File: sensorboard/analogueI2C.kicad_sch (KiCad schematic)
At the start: 51 parts, among them J1 Conn_01x03, J12 Conn_01x03, J13 Conn_01x03, J2 Conn_01x03, J3 Conn_01x03, J4 Conn_01x03, J5 Conn_01x03, J6 Conn_01x03, J7 Conn_01x03, J8 Conn_01x03, U13 ADS1219, U14 ADS1219, U15 ADS1219

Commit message: schemtiac update
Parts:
- added C25, C26, C27: 10uF, Capacitor_SMD:C_0603_1608Metric, symbol Device:C_Small
- added C28, C29, C30: 100nF, Capacitor_SMD:C_0603_1608Metric, symbol Device:C_Small
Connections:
- net +3V3: now also C25.1, C26.1, C27.1, C28.1, C29.1, C30.1
- net GND: now also C25.2, C26.2, C27.2, C28.2, C29.2, C30.2

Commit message: update
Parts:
- R29, R30, R31: value 1k -> 10k
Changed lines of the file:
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@@
     (in_bom yes) (on_board yes)
     (property "Reference" "R31" (id 0) (at 60.96 94.0816 90))
-    (property "Value" "1k" (id 1) (at 60.96 96.393 90))
+    (property "Value" "10k" (id 1) (at 60.96 96.393 90))
     (property "Footprint" "Resistor_SMD:R_0603_1608Metric" (id 2) (at 60.96 99.06 0)
       (effects (font (size 1.27 1.27)) hide)
@@
     (in_bom yes) (on_board yes)
     (property "Reference" "R30" (id 0) (at 60.96 59.7916 90))
-    (property "Value" "1k" (id 1) (at 60.96 62.103 90))
+    (property "Value" "10k" (id 1) (at 60.96 62.103 90))
     (property "Footprint" "Resistor_SMD:R_0603_1608Metric" (id 2) (at 60.96 64.77 0)
       (effects (font (size 1.27 1.27)) hide)
@@
     (in_bom yes) (on_board yes)
     (property "Reference" "R29" (id 0) (at 60.96 25.5016 90))
-    (property "Value" "1k" (id 1) (at 60.96 27.813 90))
+    (property "Value" "10k" (id 1) (at 60.96 27.813 90))
     (property "Footprint" "Resistor_SMD:R_0603_1608Metric" (id 2) (at 60.96 30.48 0)
       (effects (font (size 1.27 1.27)) hide)

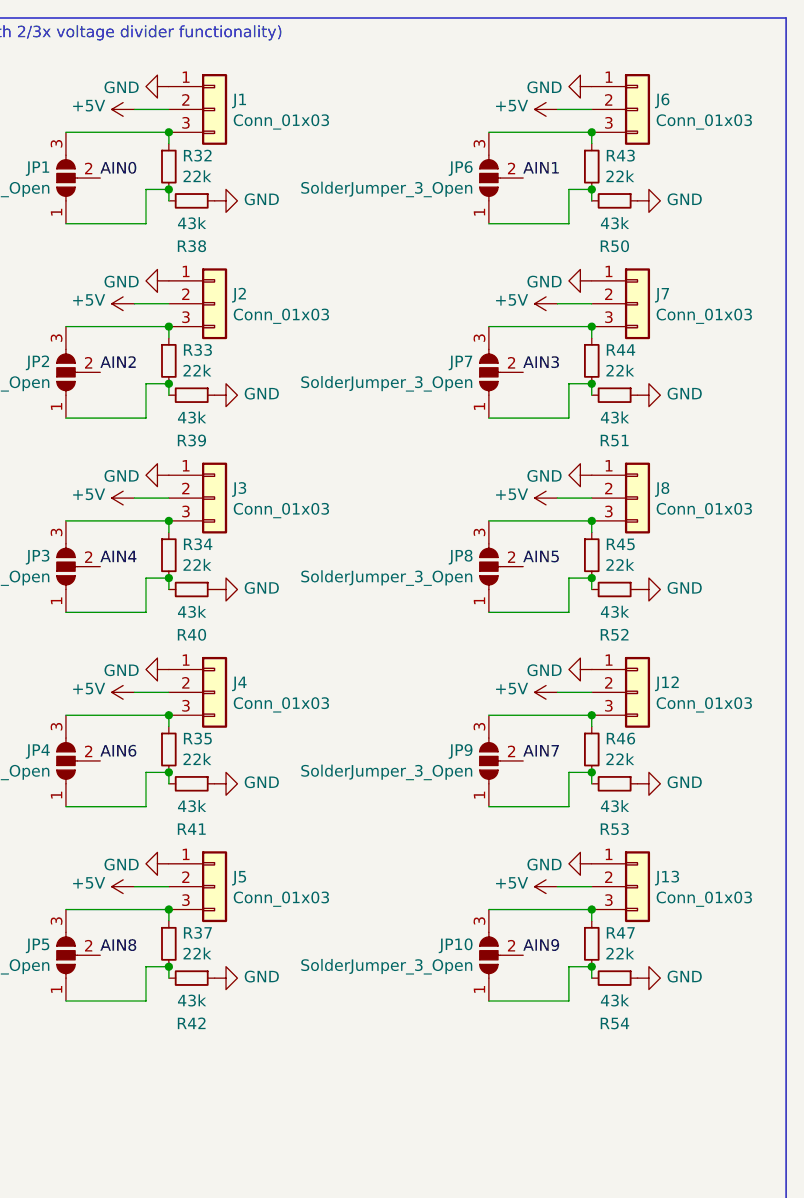
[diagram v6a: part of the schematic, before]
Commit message: Solder jumper silkscreens and moved MOSI
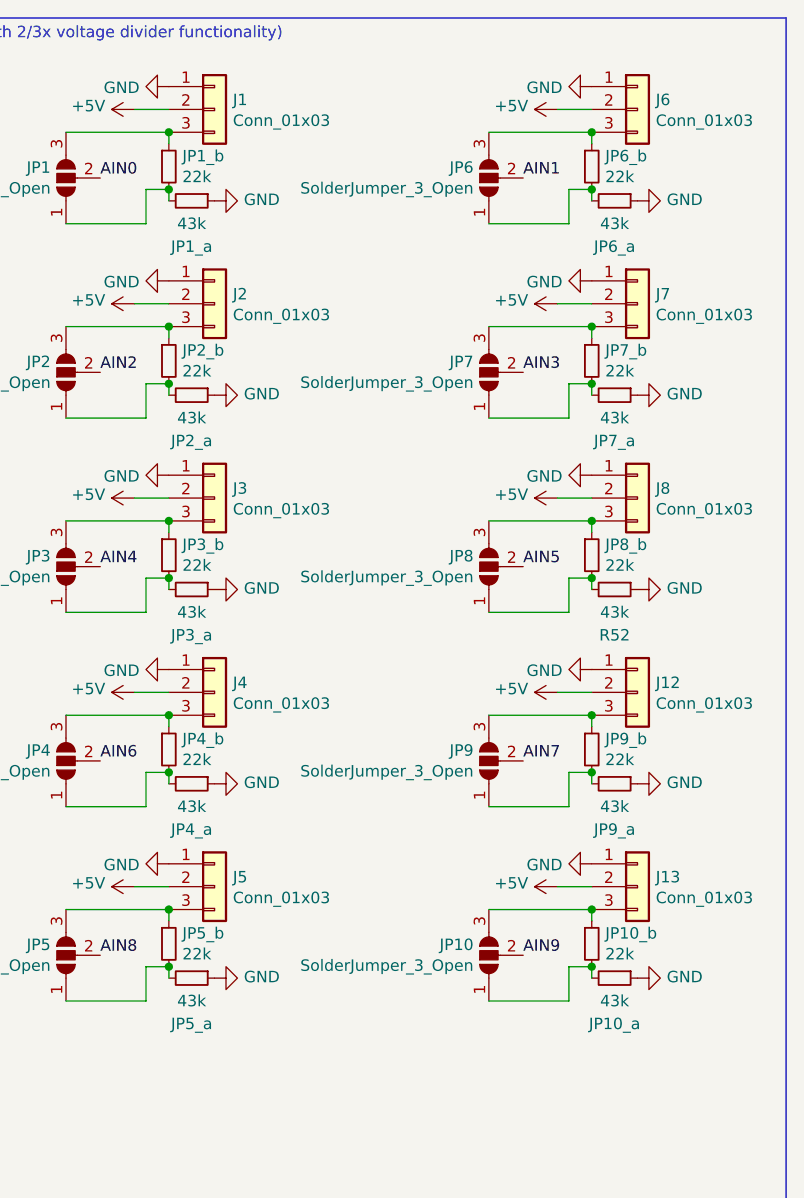
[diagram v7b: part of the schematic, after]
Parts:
- renumbered R54 to JP10_a, R47 to JP10_b, R38 to JP1_a, R32 to JP1_b, R39 to JP2_a, R33 to JP2_b, R40 to JP3_a, R34 to JP3_b, R41 to JP4_a, R35 to JP4_b, R42 to JP5_a, R37 to JP5_b, R50 to JP6_a, R43 to JP6_b, R51 to JP7_a, R44 to JP7_b, R45 to JP8_b, R53 to JP9_a, R46 to JP9_b
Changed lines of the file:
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@@
   (symbol (lib_id "Device:R_Small") (at 262.89 29.21 0) (unit 1)
     (in_bom yes) (on_board yes)
-    (property "Reference" "R43" (id 0) (at 264.3886 28.0416 0)
+    (property "Reference" "JP6_b" (id 0) (at 264.3886 28.0416 0)
       (effects (font (size 1.27 1.27)) (justify left))
     )
@@
   (symbol (lib_id "Device:R_Small") (at 265.43 33.02 270) (unit 1)
     (in_bom yes) (on_board yes)
-    (property "Reference" "R50" (id 0) (at 265.43 38.1 90))
+    (property "Reference" "JP6_a" (id 0) (at 265.43 38.1 90))
     (property "Value" "43k" (id 1) (at 265.43 35.56 90))
     (property "Footprint" "Resistor_SMD:R_0603_1608Metric" (id 2) (at 265.43 33.02 0)
@@
   (symbol (lib_id "Device:R_Small") (at 262.89 50.8 0) (unit 1)
     (in_bom yes) (on_board yes)
-    (property "Reference" "R44" (id 0) (at 264.3886 49.6316 0)
+    (property "Reference" "JP7_b" (id 0) (at 264.3886 49.6316 0)
       (effects (font (size 1.27 1.27)) (justify left))
     )
@@
   (symbol (lib_id "Device:R_Small") (at 265.43 54.61 270) (unit 1)
     (in_bom yes) (on_board yes)
-    (property "Reference" "R51" (id 0) (at 265.43 59.69 90))
+    (property "Reference" "JP7_a" (id 0) (at 265.43 59.69 90))
     (property "Value" "43k" (id 1) (at 265.43 57.15 90))
     (property "Footprint" "Resistor_SMD:R_0603_1608Metric" (id 2) (at 265.43 54.61 0)
@@
   (symbol (lib_id "Device:R_Small") (at 262.89 72.39 0) (unit 1)
     (in_bom yes) (on_board yes)
-    (property "Reference" "R45" (id 0) (at 264.3886 71.2216 0)
+    (property "Reference" "JP8_b" (id 0) (at 264.3886 71.2216 0)
       (effects (font (size 1.27 1.27)) (justify left))
     )
@@
   (symbol (lib_id "Device:R_Small") (at 262.89 93.98 0) (unit 1)
     (in_bom yes) (on_board yes)
-    (property "Reference" "R46" (id 0) (at 264.3886 92.8116 0)
+    (property "Reference" "JP9_b" (id 0) (at 264.3886 92.8116 0)
       (effects (font (size 1.27 1.27)) (justify left))
     )
@@
   (symbol (lib_id "Device:R_Small") (at 265.43 97.79 270) (unit 1)
     (in_bom yes) (on_board yes)
-    (property "Reference" "R53" (id 0) (at 265.43 102.87 90))
+    (property "Reference" "JP9_a" (id 0) (at 265.43 102.87 90))
     (property "Value" "43k" (id 1) (at 265.43 100.33 90))
     (property "Footprint" "Resistor_SMD:R_0603_1608Metric" (id 2) (at 265.43 97.79 0)
@@
   (symbol (lib_id "Device:R_Small") (at 262.89 115.57 0) (unit 1)
     (in_bom yes) (on_board yes)
-    (property "Reference" "R47" (id 0) (at 264.3886 114.4016 0)
+    (property "Reference" "JP10_b" (id 0) (at 264.3886 114.4016 0)
       (effects (font (size 1.27 1.27)) (justify left))
     )
@@
   (symbol (lib_id "Device:R_Small") (at 265.43 119.38 270) (unit 1)
     (in_bom yes) (on_board yes)
-    (property "Reference" "R54" (id 0) (at 265.43 124.46 90))
+    (property "Reference" "JP10_a" (id 0) (at 265.43 124.46 90))
     (property "Value" "43k" (id 1) (at 265.43 121.92 90))
     (property "Footprint" "Resistor_SMD:R_0603_1608Metric" (id 2) (at 265.43 119.38 0)
@@
   (symbol (lib_id "Device:R_Small") (at 215.9 29.21 0) (unit 1)
     (in_bom yes) (on_board yes)
-    (property "Reference" "R32" (id 0) (at 217.3986 28.0416 0)
+    (property "Reference" "JP1_b" (id 0) (at 217.3986 28.0416 0)
       (effects (font (size 1.27 1.27)) (justify left))
     )
@@
   (symbol (lib_id "Device:R_Small") (at 218.44 33.02 270) (unit 1)
     (in_bom yes) (on_board yes)
-    (property "Reference" "R38" (id 0) (at 218.44 38.1 90))
+    (property "Reference" "JP1_a" (id 0) (at 218.44 38.1 90))
     (property "Value" "43k" (id 1) (at 218.44 35.56 90))
     (property "Footprint" "Resistor_SMD:R_0603_1608Metric" (id 2) (at 218.44 33.02 0)
@@
   (symbol (lib_id "Device:R_Small") (at 215.9 50.8 0) (unit 1)
     (in_bom yes) (on_board yes)
-    (property "Reference" "R33" (id 0) (at 217.3986 49.6316 0)
+    (property "Reference" "JP2_b" (id 0) (at 217.3986 49.6316 0)
       (effects (font (size 1.27 1.27)) (justify left))
     )
@@
   (symbol (lib_id "Device:R_Small") (at 218.44 54.61 270) (unit 1)
     (in_bom yes) (on_board yes)
-    (property "Reference" "R39" (id 0) (at 218.44 59.69 90))
+    (property "Reference" "JP2_a" (id 0) (at 218.44 59.69 90))
     (property "Value" "43k" (id 1) (at 218.44 57.15 90))
     (property "Footprint" "Resistor_SMD:R_0603_1608Metric" (id 2) (at 218.44 54.61 0)
@@
   (symbol (lib_id "Device:R_Small") (at 215.9 72.39 0) (unit 1)
     (in_bom yes) (on_board yes)
-    (property "Reference" "R34" (id 0) (at 217.3986 71.2216 0)
+    (property "Reference" "JP3_b" (id 0) (at 217.3986 71.2216 0)
       (effects (font (size 1.27 1.27)) (justify left))
     )
@@
   (symbol (lib_id "Device:R_Small") (at 218.44 76.2 270) (unit 1)
     (in_bom yes) (on_board yes)
-    (property "Reference" "R40" (id 0) (at 218.44 81.28 90))
+    (property "Reference" "JP3_a" (id 0) (at 218.44 81.28 90))
     (property "Value" "43k" (id 1) (at 218.44 78.74 90))
     (property "Footprint" "Resistor_SMD:R_0603_1608Metric" (id 2) (at 218.44 76.2 0)
@@
   (symbol (lib_id "Device:R_Small") (at 215.9 93.98 0) (unit 1)
     (in_bom yes) (on_board yes)
-    (property "Reference" "R35" (id 0) (at 217.3986 92.8116 0)
+    (property "Reference" "JP4_b" (id 0) (at 217.3986 92.8116 0)
       (effects (font (size 1.27 1.27)) (justify left))
     )
@@
   (symbol (lib_id "Device:R_Small") (at 218.44 97.79 270) (unit 1)
     (in_bom yes) (on_board yes)
-    (property "Reference" "R41" (id 0) (at 218.44 102.87 90))
+    (property "Reference" "JP4_a" (id 0) (at 218.44 102.87 90))
     (property "Value" "43k" (id 1) (at 218.44 100.33 90))
     (property "Footprint" "Resistor_SMD:R_0603_1608Metric" (id 2) (at 218.44 97.79 0)
@@
   (symbol (lib_id "Device:R_Small") (at 215.9 115.57 0) (unit 1)
     (in_bom yes) (on_board yes)
-    (property "Reference" "R37" (id 0) (at 217.3986 114.4016 0)
+    (property "Reference" "JP5_b" (id 0) (at 217.3986 114.4016 0)
       (effects (font (size 1.27 1.27)) (justify left))
     )
@@
   (symbol (lib_id "Device:R_Small") (at 218.44 119.38 270) (unit 1)
     (in_bom yes) (on_board yes)
-    (property "Reference" "R42" (id 0) (at 218.44 124.46 90))
+    (property "Reference" "JP5_a" (id 0) (at 218.44 124.46 90))
     (property "Value" "43k" (id 1) (at 218.44 121.92 90))
     (property "Footprint" "Resistor_SMD:R_0603_1608Metric" (id 2) (at 218.44 119.38 0)
